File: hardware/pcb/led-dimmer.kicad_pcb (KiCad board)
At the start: 2 copper layers, 42 x 13.6 mm, 17 parts, among them J1 Conn_01x01, J2 Conn_01x01, J3 1984633, J4 74651175R, J5 74651175R, Q2 DMP3013SFV, U1 MIC1555YM5-TR

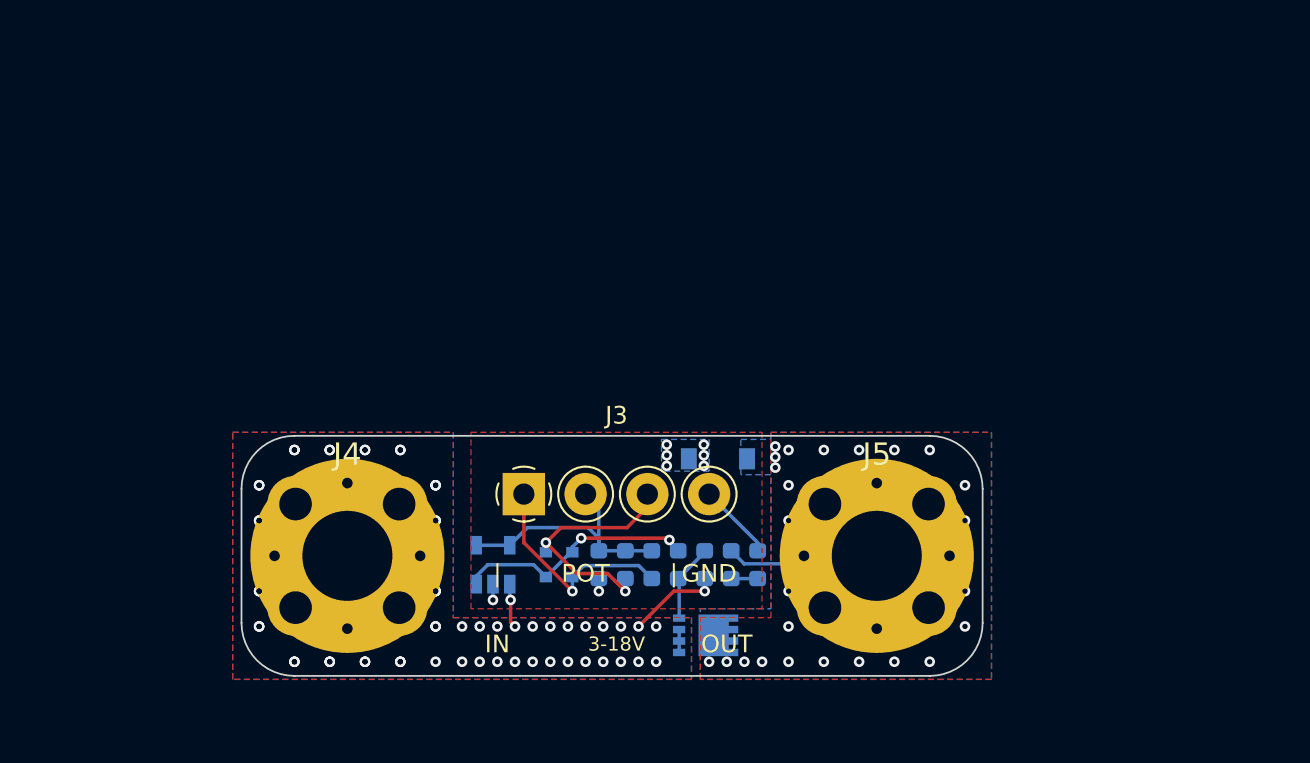
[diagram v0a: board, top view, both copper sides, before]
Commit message: Schematic done
Made some of the footprint and layout.
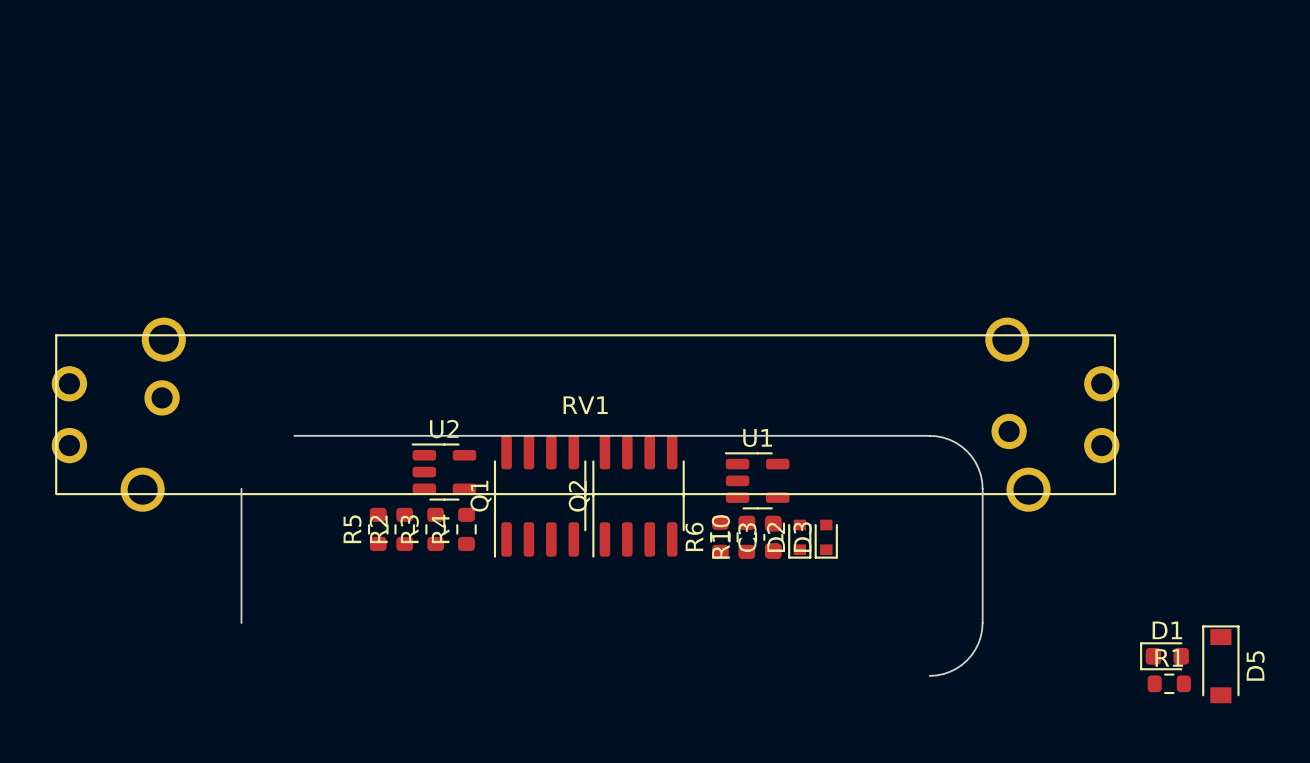
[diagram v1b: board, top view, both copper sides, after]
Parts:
- removed J1, J2: Conn_01x01, MountingHole:MountingHole_5.5mm_Pad_Via
- removed J3: 1984633, TerminalBlock_4Ucon:TerminalBlock_4Ucon_1x04_P3.50mm_Horizontal
- removed J4, J5: 74651175R, connectors:M5_74651175R_Solder
- removed R7, R8: R, Resistor_SMD:R_0603_1608Metric
- removed R9: 100k, Resistor_SMD:R_0603_1608Metric
- added Q1: Q_PMOS_SGD, led_dimmer:SI4143DY-T1-GE3, F.Cu at (145.9, 96.6)
- added R2: 1k, Resistor_SMD:R_0603_1608Metric, F.Cu at (138.2, 98.5)
- added R3: 100, Resistor_SMD:R_0603_1608Metric, F.Cu at (140.0, 98.5)
- added R4: 100k, Resistor_SMD:R_0603_1608Metric, F.Cu at (141.8, 98.5)
- added R5: 100k, Resistor_SMD:R_0603_1608Metric, F.Cu at (136.8, 98.5)
- added R6: 100k, Resistor_SMD:R_0603_1608Metric, F.Cu at (156.1, 99.0)
- added RV1: R_Potentiometer_Dual, led_dimmer:PTA4544-2010CIB103, F.Cu at (148.5, 92.0)
- added U2: OPAMP, Package_TO_SOT_SMD:SOT-23-5, F.Cu at (140.5, 95.2)
- C3, D1, D2, D3, D5, R1, R10, U1: moved to F.Cu
- Q2: value DMP3013SFV -> Q_PMOS_SGD; footprint Package_SON:Diodes_PowerDI3333-8 -> led_dimmer:SI4143DY-T1-GE3; moved to F.Cu
- moved D5 30.8 mm to (184.5, 106.2), turned to -90 degrees
- moved R1 25.7 mm to (181.6, 107.2), turned to 0 degrees
- moved D1 23.8 mm to (181.5, 105.7), turned to 0 degrees
- moved D3 16.0 mm to (162.1, 99.0)
- moved U1 15.7 mm to (158.2, 95.8), turned to 0 degrees
- moved D2 13.0 mm to (160.6, 99.0)
- moved C3 10.0 mm to (159.1, 99.0), turned to 90 degrees
- moved Q2 8.77 mm to (151.5, 96.6), turned to 90 degrees
- moved R10 4.19 mm to (157.6, 99.0)
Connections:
- net /TRG_THR renamed POT_OUT
- D2 pad 1: Net-(D2-Pad1) -> POT_H
- D3 pad 2: Net-(D3-Pad2) -> POT_L
- D5 pad 1: /LED_OUT -> LED_OUT
- Q2 pad 1: Net-(Q2-Pad1) -> Net-(R6-Pad1)
- Q2 pad 2: Net-(Q2-Pad1) -> Net-(R10-Pad1)
- Q2 pad 3: Net-(Q2-Pad1) -> LED_OUT
- R1 pad 1: /LED_OUT -> LED_OUT
- R10 pad 1: /GATE -> Net-(R10-Pad1)
- U1 pad 1: +12V -> Net-(R6-Pad1)
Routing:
- net POT_OUT: track 15.0 -> 0.00 mm
- net Net-(D3-Pad2): track 14.2 -> 0.00 mm, vias 2 -> 0
- net /PWM: track 14.0 -> 0.00 mm, vias 2 -> 0
- net Net-(D2-Pad1): track 12.5 -> 0.00 mm, vias 1 -> 0
- net /LED_OUT: track 8.74 -> 0.00 mm, vias 25 -> 0
- net +12V: track 7.89 -> 0.00 mm, vias 59 -> 0
- net GND: track 5.96 -> 0.00 mm, vias 8 -> 0
- net /GATE: track 4.45 -> 0.00 mm
- net Net-(D1-Pad2): track 1.50 -> 0.00 mm
- net Net-(Q2-Pad1): track 1.30 -> 0.00 mm
- removed copper zone on B.Cu, net +12V
- removed copper zone on F.Cu, net +12V
- removed copper zone on B.Cu, net /LED_OUT
- removed copper zone on F.Cu, net /LED_OUT
- removed copper zone on B.Cu, net GND
- removed copper zone on F.Cu, net GND
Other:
- outline, holes or cut-outs redrawn
- board text removed: "21.05.16 Rev 1"
- board text removed: "3-18V"
- board text removed: "GND"
- board text removed: "IN"
- board text removed: "OUT"
- board text removed: "POT"
- board text removed: "|"

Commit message: First release
A first release which is ordered from JLC.
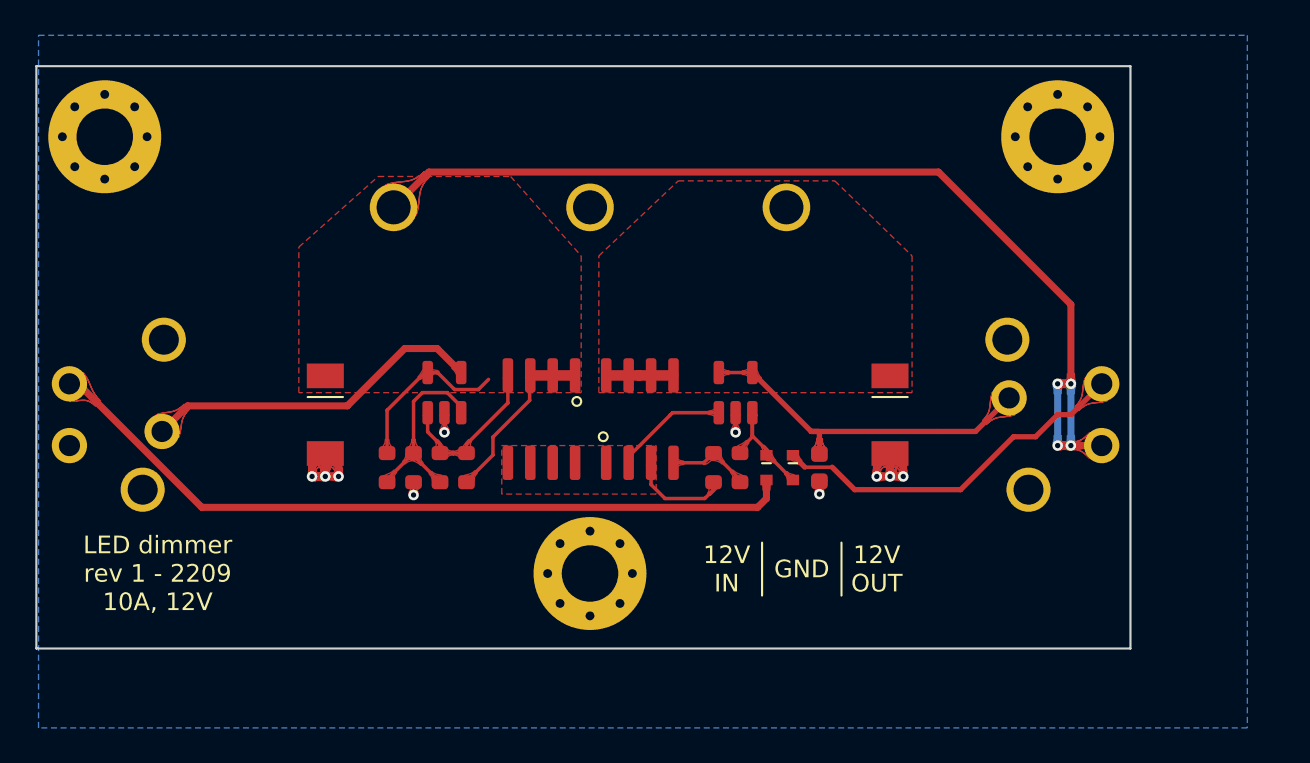
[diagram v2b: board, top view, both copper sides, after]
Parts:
- removed D1: LED, LED_SMD:LED_0603_1608Metric
- removed R1: 2k, Resistor_SMD:R_0603_1608Metric
- added D4: D_Zener, Diode_SMD:D_SOD-128, F.Cu at (133.8, 92.0)
- added H1: MountingHole, MountingHole:MountingHole_3.2mm_M3_Pad_Via, F.Cu at (148.8, 101.0)
- added H2: MountingHole, MountingHole:MountingHole_3.2mm_M3_Pad_Via, F.Cu at (175.2, 76.2)
- added H3: MountingHole, MountingHole:MountingHole_3.2mm_M3_Pad_Via, F.Cu at (121.2, 76.2)
- added J1: 386307803, led_dimmer:386307803, F.Cu at (148.8, 80.2)
- D5: value D_Schottky -> D_Zener; footprint Diode_SMD:D_SOD-123 -> Diode_SMD:D_SOD-128
- RV1: value R_Potentiometer_Dual -> PTA4544-2010CIB103; moved to B.Cu
- U2: value OPAMP -> TL081HIDBVR
- moved D5 23.6 mm to (165.8, 92.0)
- moved R5 6.10 mm to (141.8, 95.0)
- moved D3 5.20 mm to (158.8, 95.0), turned to -90 degrees
- moved U1 5.15 mm to (157.0, 90.8), turned to 90 degrees
- moved C3 4.74 mm to (161.8, 95.0), turned to -90 degrees
- moved U2 4.50 mm to (140.5, 90.8), turned to 90 degrees
- moved Q1 4.35 mm to (146.0, 92.2), turned to -90 degrees
- moved Q2 4.35 mm to (151.6, 92.2)
- moved D2 3.97 mm to (160.2, 95.0), turned to -90 degrees
- moved R10 3.97 mm to (157.2, 95.0)
- moved R6 3.97 mm to (155.8, 95.0)
- moved R4 3.81 mm to (140.2, 95.0)
- moved R3 3.72 mm to (138.8, 95.0)
- moved R2 3.64 mm to (137.2, 95.0)
- turned RV1 to 180 degrees
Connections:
- R2 pad 2: /Vin -> +12V
- RV1 pad 4: /Vin -> +12V
- U2 pad 5: /Vin -> +12V
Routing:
- net +12V: track 0.00 -> 77.4 mm, vias 0 -> 4
- net POT_L: track 0.00 -> 43.7 mm
- net POT_H: track 0.00 -> 20.8 mm
- net POT_OUT: track 0.00 -> 20.3 mm
- net POT2_OUT: track 0.00 -> 19.5 mm
- net GND: track 0.00 -> 16.5 mm, vias 0 -> 10
- net Net-(R6-Pad1): track 0.00 -> 12.2 mm
- net Net-(R2-Pad1): track 0.00 -> 11.1 mm
- net Net-(R4-Pad2): track 0.00 -> 9.10 mm
- net /PWM: track 0.00 -> 7.40 mm
- net Net-(R10-Pad1): track 0.00 -> 4.77 mm
- net LED_OUT: track 0.00 -> 3.81 mm
- added copper zone on F.Cu, net +12V
- added copper zone on B.Cu, net GND
- added copper zone on F.Cu, net LED_OUT
- added copper zone on F.Cu, net Net-(R6-Pad1)
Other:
- board size 42 x 13.6 mm -> 62 x 33 mm
- board text added: "12V IN"
- board text added: "12V OUT"
- board text added: "GND"
- board text added: "LED dimmer rev 1 - 2209 10A, 12V"
